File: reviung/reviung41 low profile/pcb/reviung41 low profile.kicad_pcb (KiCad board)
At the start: 2 copper layers, 251.3 x 103.7 mm, 101 parts, among them SW1 SW_PUSH, SW10 SW_PUSH, SW11 SW_PUSH, SW12 SW_PUSH, SW13 SW_PUSH, SW14 SW_PUSH, SW15 SW_PUSH, SW16 SW_PUSH, SW17 SW_PUSH, SW18 SW_PUSH, SW19 SW_PUSH, SW2 SW_PUSH, SW20 SW_PUSH, SW21 SW_PUSH, SW22 SW_PUSH, SW23 SW_PUSH, SW24 SW_PUSH, SW25 SW_PUSH, SW26 SW_PUSH, SW27 SW_PUSH, SW28 SW_PUSH, SW29 SW_PUSH, SW3 SW_PUSH, SW30 SW_PUSH, SW31 SW_PUSH, SW32 SW_PUSH, SW33 SW_PUSH, SW34 SW_PUSH, SW35 SW_PUSH, SW36 SW_PUSH, SW37 SW_PUSH, SW38 SW_PUSH, SW39 SW_2U_PUSH, SW4 SW_PUSH, SW40 SW_PUSH, SW41 SW_PUSH, SW5 SW_PUSH, SW6 SW_PUSH, SW7 SW_PUSH, SW8 SW_PUSH, SW9 SW_PUSH, U1 ProMicro

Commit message: reviung41/low profile: bump version
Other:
- board text added: "reviung41 low profile github.com/idank/keyboards@459c026"
- board text removed: "reviung41 low profile github.com/idank/keyboards"
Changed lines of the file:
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@@
     (fp_arc (start -56.831058 -0.000001) (mid -54.566994 0.128562) (end -52.332037 0.512598)
       (stroke (width 0.2) (type solid)) (layer "Edge.Cuts"))
-    (fp_arc (start -43.903779 85.253334) (mid -43.281265 85.470726) (end -42.929409 86.028383)
+    (fp_arc (start -43.903779 85.253334) (mid -43.281264 85.470726) (end -42.929409 86.028383)
       (stroke (width 0.2) (type solid)) (layer "Edge.Cuts"))
     (fp_arc (start -41.178247 91.116827) (mid -41.660403 90.849564) (end -41.927666 90.367408)
@@
     (fp_arc (start 37.146773 4.018393) (mid 36.696871 4.069653) (end 36.246969 4.018393)
       (stroke (width 0.2) (type solid)) (layer "Edge.Cuts"))
-    (fp_arc (start 41.927666 90.367408) (mid 41.660326 90.849478) (end 41.178247 91.116827)
+    (fp_arc (start 41.927666 90.367408) (mid 41.660311 90.849463) (end 41.178247 91.116827)
       (stroke (width 0.2) (type solid)) (layer "Edge.Cuts"))
-    (fp_arc (start 42.929409 86.028383) (mid 43.281247 85.470724) (end 43.903779 85.253334)
+    (fp_arc (start 42.929409 86.028383) (mid 43.281263 85.470738) (end 43.903779 85.253334)
       (stroke (width 0.2) (type solid)) (layer "Edge.Cuts"))
     (fp_arc (start 52.332038 0.512599) (mid 54.566994 0.128554) (end 56.831059 0)
@@
     (fp_arc (start 59.465859 67.164153) (mid 59.683265 66.541653) (end 60.240908 66.189783)
       (stroke (width 0.2) (type solid)) (layer "Edge.Cuts"))
-    (fp_arc (start 59.465859 84.253334) (mid 59.172717 84.96017) (end 58.465859 85.253334)
+    (fp_arc (start 59.465859 84.253334) (mid 59.172688 84.960141) (end 58.465859 85.253334)
       (stroke (width 0.2) (type solid)) (layer "Edge.Cuts"))
     (fp_arc (start 85.640773 60.325762) (mid 87.87573 59.941726) (end 90.139794 59.813163)
       (stroke (width 0.2) (type solid)) (layer "Edge.Cuts"))
-    (fp_arc (start 109.581168 59.300564) (mid 107.346212 59.684601) (end 105.082147 59.813163)
+    (fp_arc (start 109.581168 59.300564) (mid 107.346211 59.684597) (end 105.082147 59.813163)
       (stroke (width 0.2) (type solid)) (layer "Edge.Cuts"))
-    (fp_arc (start 112.256245 -0.000001) (mid 112.878736 0.217408) (end 113.230615 0.775048)
+    (fp_arc (start 112.256245 -0.000001) (mid 112.878761 0.217399) (end 113.230615 0.775048)
       (stroke (width 0.2) (type solid)) (layer "Edge.Cuts"))
     (fp_arc (start 125.648939 54.564722) (mid 125.52263 55.319602) (end 124.899521 55.764044)
@@
     (pad "" np_thru_hole circle (at 0 0 180) (size 2.3 2.3) (drill 2.3) (layers "*.Cu" "*.Mask"))
   )
-  (gr_text "reviung41 low profile\ngithub.com/idank/keyboards" (at 149.13 41.08 347) (layer "B.SilkS")
+  (gr_text "reviung41 low profile\ngithub.com/idank/keyboards@459c026" (at 149.13 41.08 347) (layer "B.SilkS")
     (effects (font (size 1 1.2) (thickness 0.2)) (justify mirror))
   )

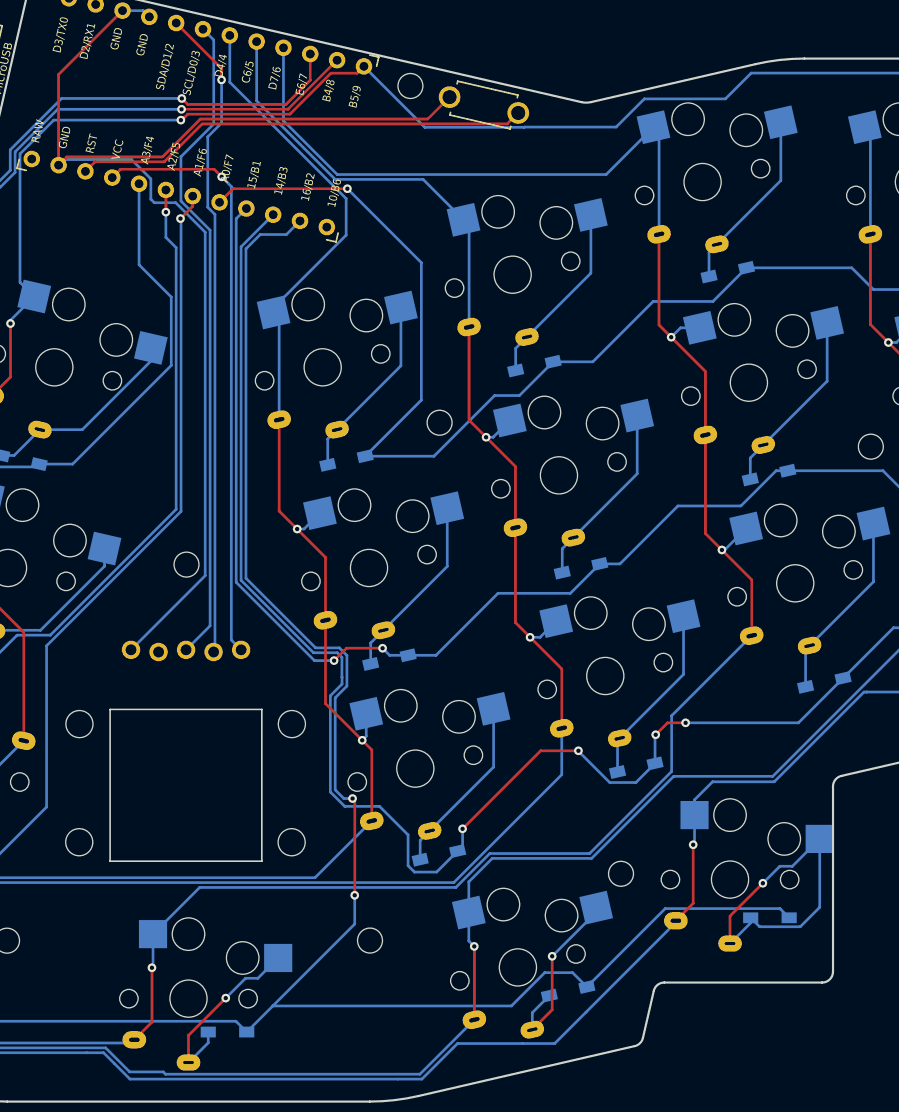
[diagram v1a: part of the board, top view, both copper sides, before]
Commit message: reviung low profile: add top plate
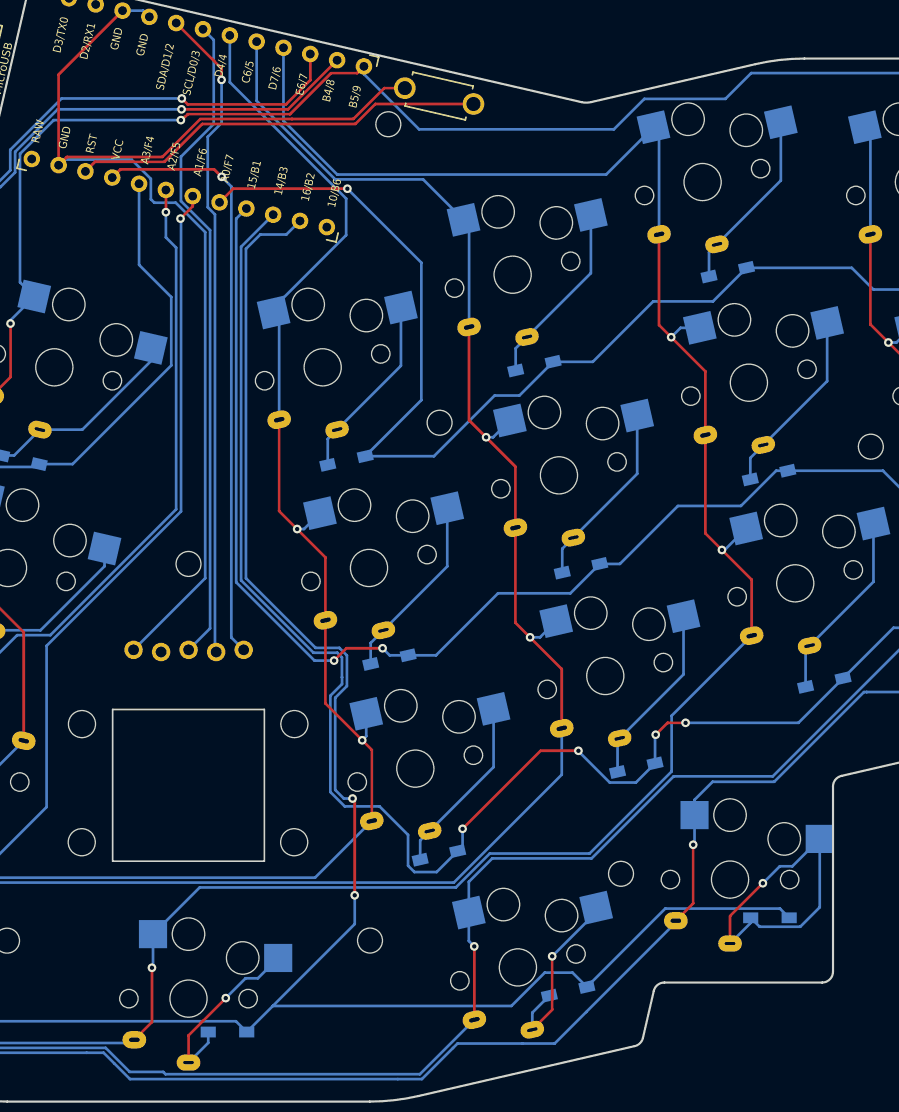
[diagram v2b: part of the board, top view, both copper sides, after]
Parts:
- moved RESET1 4.21 mm to (170.9, 39.8)
- moved REF** 4.08 mm to (166.2, 42.4)
- moved U2 0.23 mm to (152.9, 90.4)
- moved REF** 0.19 mm to (147.8, 91.0)
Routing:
- net GND: track 117.1 -> 113.2 mm
- net reset: track 42.2 -> 38.4 mm
- net col5: track 259.0 -> 259.6 mm

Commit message: reviung lp: bump version
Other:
- board text added: "reviung41 low profile github.com/idank/keyboards@34bbc3b"
- board text removed: "reviung41 low profile github.com/idank/keyboards@459c026"
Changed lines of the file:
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@@
     (fp_arc (start -56.831058 -0.000001) (mid -54.566994 0.128562) (end -52.332037 0.512598)
       (stroke (width 0.2) (type solid)) (layer "Edge.Cuts"))
-    (fp_arc (start -43.903779 85.253334) (mid -43.281264 85.470726) (end -42.929409 86.028383)
+    (fp_arc (start -43.903779 85.253334) (mid -43.281265 85.470726) (end -42.929409 86.028383)
       (stroke (width 0.2) (type solid)) (layer "Edge.Cuts"))
     (fp_arc (start -41.178247 91.116827) (mid -41.660403 90.849564) (end -41.927666 90.367408)
@@
     (fp_arc (start 37.146773 4.018393) (mid 36.696871 4.069653) (end 36.246969 4.018393)
       (stroke (width 0.2) (type solid)) (layer "Edge.Cuts"))
-    (fp_arc (start 41.927666 90.367408) (mid 41.660281 90.849433) (end 41.178247 91.116827)
+    (fp_arc (start 41.927666 90.367408) (mid 41.660266 90.849418) (end 41.178247 91.116827)
       (stroke (width 0.2) (type solid)) (layer "Edge.Cuts"))
-    (fp_arc (start 42.929409 86.028383) (mid 43.28127 85.470714) (end 43.903779 85.253334)
+    (fp_arc (start 42.929409 86.028383) (mid 43.281254 85.4707) (end 43.903779 85.253334)
       (stroke (width 0.2) (type solid)) (layer "Edge.Cuts"))
     (fp_arc (start 52.332038 0.512599) (mid 54.566994 0.128554) (end 56.831059 0)
@@
     (fp_arc (start 59.465859 67.164153) (mid 59.683265 66.541653) (end 60.240908 66.189783)
       (stroke (width 0.2) (type solid)) (layer "Edge.Cuts"))
-    (fp_arc (start 59.465859 84.253334) (mid 59.17263 84.960083) (end 58.465859 85.253334)
+    (fp_arc (start 59.465859 84.253334) (mid 59.1726 84.960053) (end 58.465859 85.253334)
       (stroke (width 0.2) (type solid)) (layer "Edge.Cuts"))
     (fp_arc (start 85.640773 60.325762) (mid 87.87573 59.941726) (end 90.139794 59.813163)
       (stroke (width 0.2) (type solid)) (layer "Edge.Cuts"))
-    (fp_arc (start 109.581168 59.300564) (mid 107.346211 59.684594) (end 105.082147 59.813163)
+    (fp_arc (start 109.581168 59.300564) (mid 107.346211 59.684598) (end 105.082147 59.813163)
       (stroke (width 0.2) (type solid)) (layer "Edge.Cuts"))
-    (fp_arc (start 112.256245 -0.000001) (mid 112.878761 0.217399) (end 113.230615 0.775048)
+    (fp_arc (start 112.256245 -0.000001) (mid 112.878736 0.217408) (end 113.230615 0.775048)
       (stroke (width 0.2) (type solid)) (layer "Edge.Cuts"))
     (fp_arc (start 125.648939 54.564722) (mid 125.52263 55.319602) (end 124.899521 55.764044)
@@
     (pad "" np_thru_hole circle (at 0 0 180) (size 2.3 2.3) (drill 2.3) (layers "*.Cu" "*.Mask"))
   )
-  (gr_text "reviung41 low profile\ngithub.com/idank/keyboards@459c026" (at 149.13 41.08 347) (layer "B.SilkS")
+  (gr_text "reviung41 low profile\ngithub.com/idank/keyboards@34bbc3b" (at 149.13 41.08 347) (layer "B.SilkS")
     (effects (font (size 1 1.2) (thickness 0.2)) (justify mirror))
   )
